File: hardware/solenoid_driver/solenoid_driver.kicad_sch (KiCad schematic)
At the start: 10 parts, among them J1 from_mainboard, J2 12V power, J3 to_solenoid2, J4 to_solenoid1, Q1 Q_NMOS_GDS, Q2 Q_NMOS_GDS

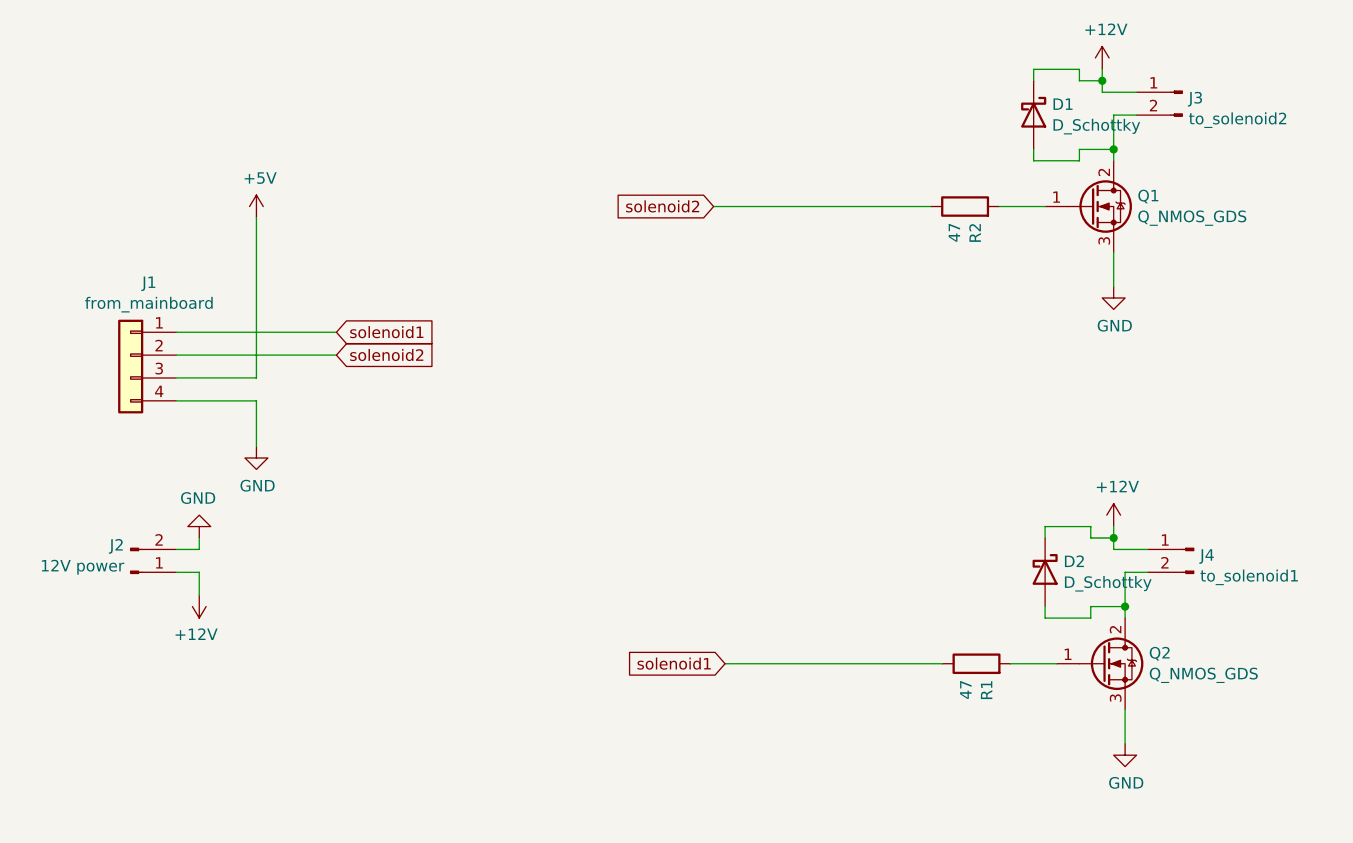
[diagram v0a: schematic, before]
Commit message: update solenoid driver
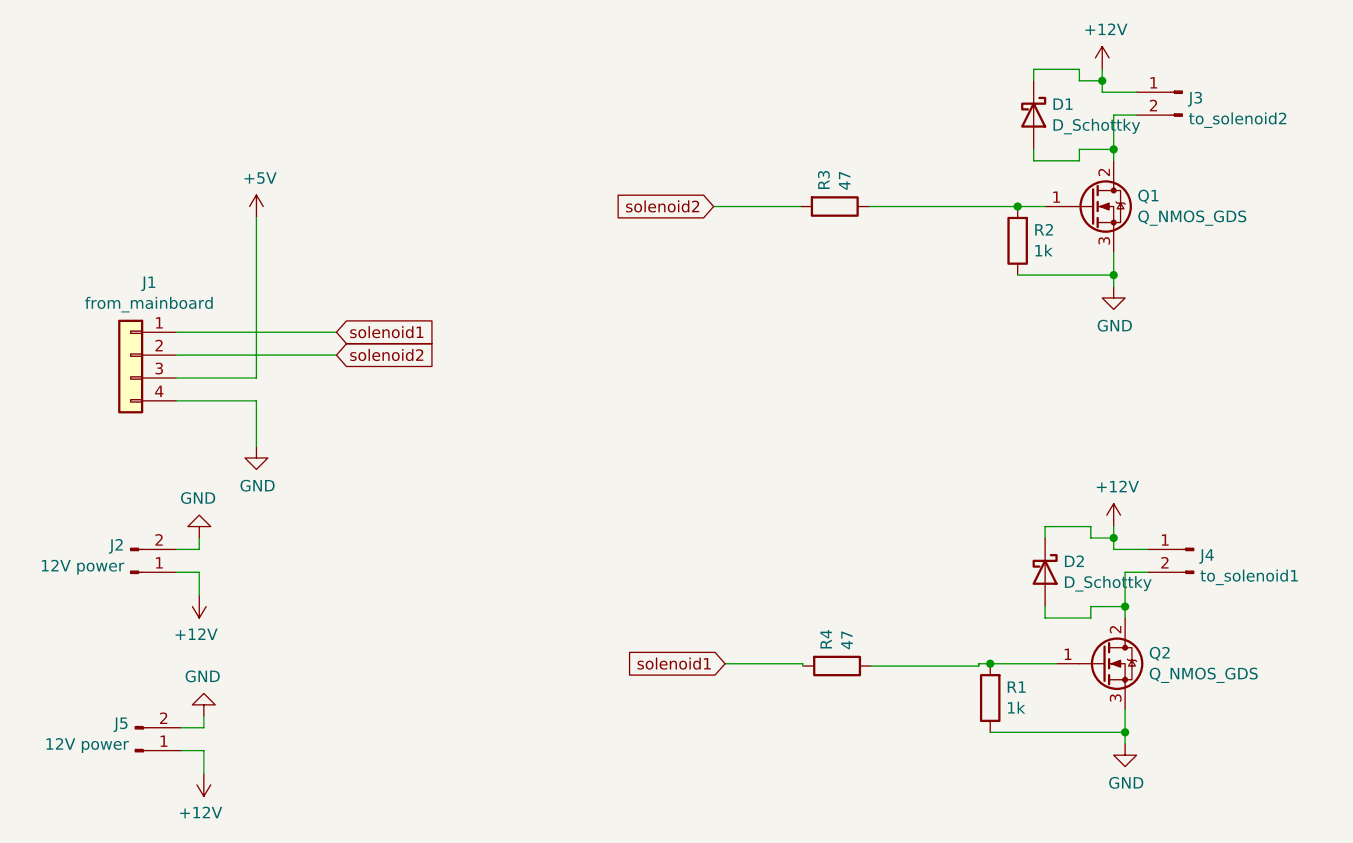
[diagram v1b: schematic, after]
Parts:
- added J5: 12V power, Connector_JST:JST_XH_B2B-XH-A_1x02_P2.50mm_Vertical, symbol Connector:Conn_01x02_Male
- added R3, R4: 47, Resistor_THT:R_Box_L13.0mm_W4.0mm_P9.00mm, symbol Device:R
- R1, R2: value 47 -> 1k
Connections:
- net +12V: now also J5.1 (Pin_1)
- net GND: now also R1.1, R2.1, J5.2 (Pin_2)
- net solenoid1: now also R4.2; no longer R1.1
- net solenoid2: now also R3.2; no longer R2.1
- net at Q2.1 (G), R1.2: now also R4.1
- net at Q1.1 (G), R2.2: now also R3.1
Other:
- moved on the sheet: R1, R2
